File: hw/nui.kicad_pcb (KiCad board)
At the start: 2 copper layers, 50.8 x 71.1 mm, 24 parts, among them J1 D_PWR, J2 IR_RCV, J3 A_PWR, J4 Input, J5 Output, U1 Teensy-LC, U2 TC7660S, U3 PGA2311

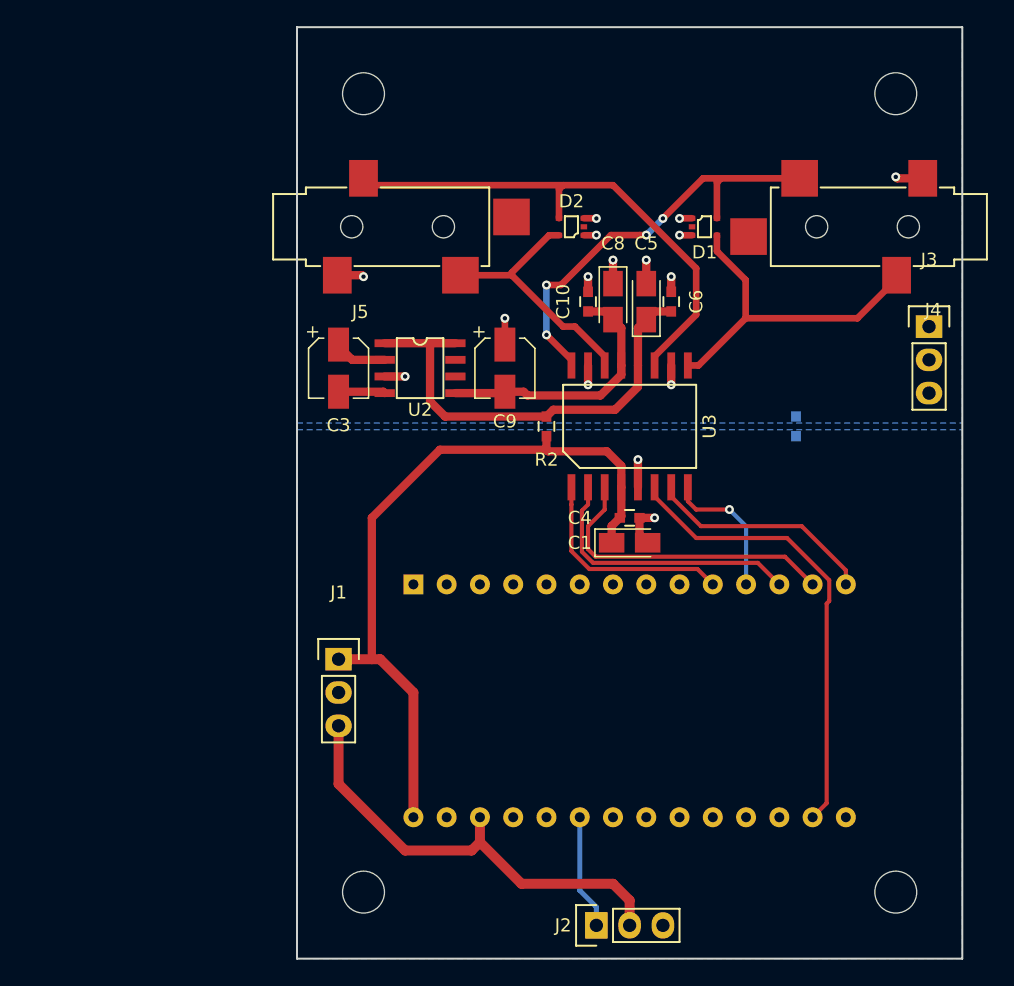
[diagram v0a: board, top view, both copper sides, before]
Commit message: Layout done for v0.0.1
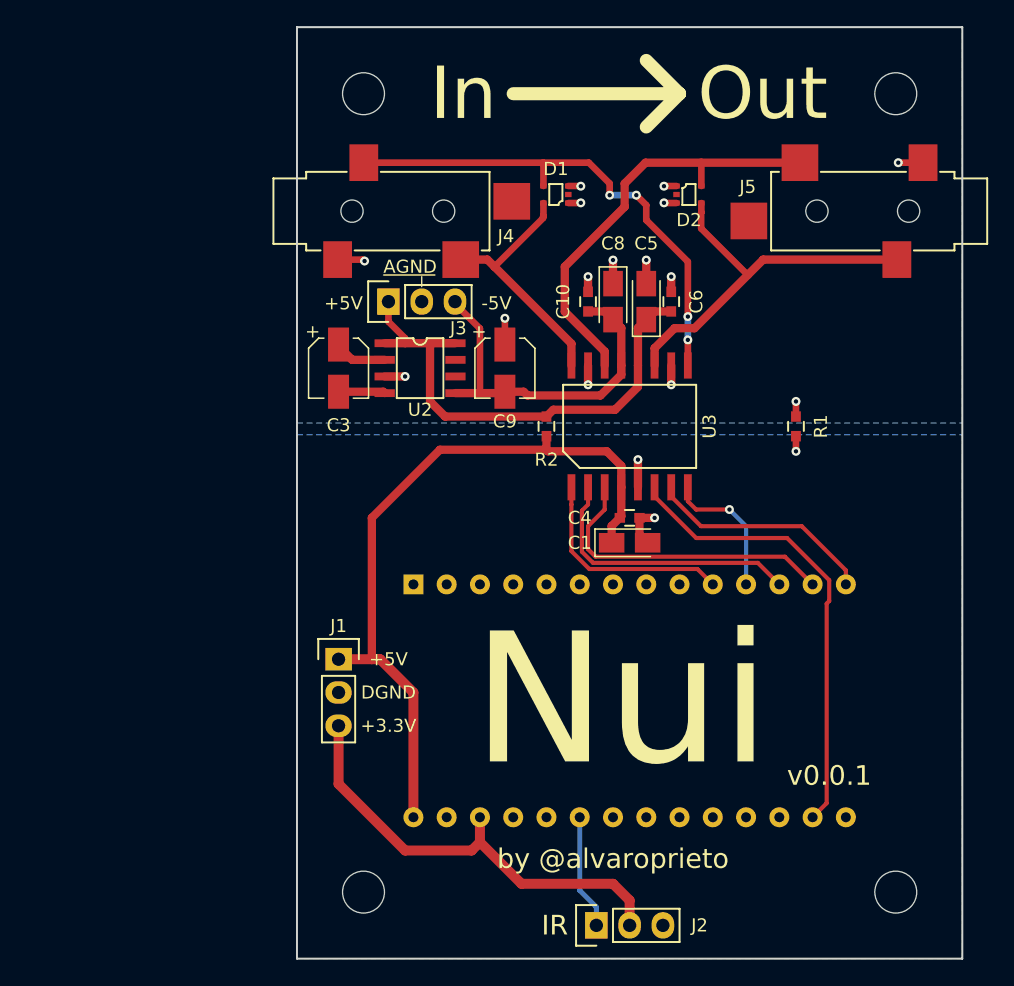
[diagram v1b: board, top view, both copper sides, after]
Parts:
- R1: moved to F.Cu
- moved J3 41.3 mm to (184.8, 76.8), turned to 90 degrees
- moved J5 35.5 mm to (221.0, 69.9), turned to 180 degrees
- moved J4 35.5 mm to (185.5, 69.9), turned to 0 degrees
- moved D1 11.6 mm to (197.6, 68.7), turned to 180 degrees
- moved D2 9.30 mm to (207.7, 68.7), turned to 0 degrees
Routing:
- net /VIN_L: track 32.8 -> 19.2 mm, vias 4 -> 0
- net /VOUT_L: track 19.3 -> 32.9 mm
- net /VIN_R: track 26.2 -> 38.8 mm, vias 0 -> 4
- net /VOUT_R: track 39.6 -> 29.6 mm
- net /VA_M: track 20.1 -> 27.9 mm
- net /VA_P: track 34.7 -> 38.4 mm
- net GNDD: track 5.43 -> 6.58 mm, vias 2 -> 3
- net GNDA: track 20.4 -> 21.4 mm, vias 14 -> 15
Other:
- board text added: "+3.3V"
- board text added: "+5V"
- board text added: "-5V"
- board text added: "AGND"
- board text added: "DGND"
- board text added: "IR"
- board text added: "In"
- board text added: "Nui"
- board text added: "Out"
- board text added: "by @alvaroprieto"
- board text added: "v0.0.1"

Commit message: Start updating pcb with new design
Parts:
- added C11: 2.2uF, Capacitors_SMD:C_0603, F.Cu at (186.2, 82.0)
- added C2: 4.7uF, Capacitors_SMD:C_0805, F.Cu at (194.6, 80.3)
- added C7: 2.2uF, Capacitors_SMD:C_0402_NoSilk, F.Cu at (183.9, 81.5)
- added R3: 10k, Resistors_SMD:R_0402_NoSilk, F.Cu at (180.9, 79.5)
- added R4: 1.74M, Resistors_SMD:R_0402_NoSilk, F.Cu at (183.4, 77.5)
- added R5: 549k, Resistors_SMD:R_0402_NoSilk, F.Cu at (183.4, 79.2)
- added R6: 511k, Resistors_SMD:R_0402_NoSilk, F.Cu at (181.9, 84.0)
- added R7: 1.58M, Resistors_SMD:R_0402_NoSilk, F.Cu at (181.9, 82.3)
- C3: value 10uF -> 1uF; footprint Capacitors_SMD:CP_Elec_4x5.3 -> Capacitors_SMD:C_1210
- C9: value 10uF -> 2.2uF; footprint Capacitors_SMD:CP_Elec_4x5.3 -> Capacitors_SMD:C_0603
- U2: value TC7660S -> LM27762; footprint alvarop:TC7660S-SOIC -> alvarop:LM27762
- moved J3 26.3 mm to (158.8, 73.2)
- moved C3 10.3 mm to (191.3, 81.3)
- moved C9 8.98 mm to (186.2, 77.0), turned to 180 degrees
- moved U2 2.62 mm to (186.2, 79.5)
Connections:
- C1 pad 1: /VD_P -> /EN+
- C4 pad 1: /VD_P -> /EN+
- C9 pad 1: GNDA -> /OUT+
- C9 pad 2: /VA_M -> GNDA
- J1 pad 1: /VD_P -> /EN+
- U1 pad 28: /VD_P -> /EN+
- U2 pad 1: /VA_P -> Net-(R3-Pad1)
- U2 pad 2: Net-(C3-Pad1) -> /FB+
- U2 pad 3: GNDA -> /EN+
- U2 pad 4: Net-(C3-Pad2) -> GNDA
- U2 pad 5: /VA_M -> Net-(C7-Pad1)
- U2 pad 6: Net-(U2-Pad6) -> /OUT-
- U2 pad 7: Net-(U2-Pad7) -> /FB-
- U2 pad 8: /VA_P -> /EN+
- U3 pad 4: /VD_P -> /EN+
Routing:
- net /VA_P: track 38.4 -> 15.5 mm
- net /VA_M: track 27.9 -> 8.87 mm
- net /VD_P: track 56.0 -> 37.8 mm
- net /EN+: track 0.00 -> 18.2 mm
- net Net-(C3-Pad1): track 4.13 -> 0.00 mm
- net Net-(C3-Pad2): track 3.69 -> 0.00 mm
- net GNDA: track 21.4 -> 17.9 mm, vias 15 -> 13

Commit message: Update Nui 1.0.0 to use nrf52810 and LM27762
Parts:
- added AE1: Antenna, alvarop:AMCA31-2R450G-S1F-T3, F.Cu at (202.7, 113.8)
- added C12: 0.1uF, Capacitors_SMD:C_0603, F.Cu at (208.0, 97.9)
- added C13: 0.1uF, Capacitors_SMD:C_0603, F.Cu at (199.4, 98.8)
- added C14: 4.7uF, Capacitors_SMD:C_0603, F.Cu at (208.0, 99.6)
- added C15: 1uF, Capacitors_SMD:C_0603, F.Cu at (208.0, 100.8)
- added C16: 0.1uF, Capacitors_SMD:C_0603, F.Cu at (208.0, 103.4)
- added C17: 12pf, Capacitors_SMD:C_0603, F.Cu at (208.0, 109.0)
- added C18: 100pf, Capacitors_SMD:C_0603, F.Cu at (205.0, 107.1)
- added C19: 12pf, Capacitors_SMD:C_0603, F.Cu at (208.0, 104.9)
- added C20: 1uF, Capacitors_SMD:C_0603, F.Cu at (187.1, 97.8)
- added C21: 1uF, Capacitors_SMD:C_0603, F.Cu at (192.5, 97.8)
- added C22: DNP, Capacitors_SMD:C_0402_NoSilk, F.Cu at (202.1, 108.0)
- added C23: DNP, Capacitors_SMD:C_0402_NoSilk, F.Cu at (202.1, 110.4)
- added D3: TVS, Diodes_SMD:D_0603, F.Cu at (184.4, 95.1)
- added F1: 2450FM07A0029T, alvarop:2450FM07A0029T, F.Cu at (202.7, 105.8)
- added J6: USB_OTG, alvarop:USB_MICRO_B, F.Cu at (181.9, 94.5)
- added J7: ARM-SWD, alvarop:ARM_SWD_SMD, B.Cu at (194.7, 104.5)
- added L1: Filter, Resistors_SMD:R_0603, F.Cu at (182.6, 100.6)
- added L2: Filter, Resistors_SMD:R_0603, F.Cu at (185.2, 92.8)
- added U4: MIC550X, alvarop:SOT-23(M5), F.Cu at (189.8, 97.9)
- added Y1: 32Mhz, Crystals:Crystal_SMD_2016-4pin_2.0x1.6mm, F.Cu at (208.0, 106.9)
- R2: footprint Capacitors_SMD:C_0603 -> Resistors_SMD:R_0402_NoSilk
- U1: value Teensy-LC -> NRF52810-QCAA; footprint alvarop:Teensy-LC -> alvarop:NRF52810_QCAA_QFN32; moved to F.Cu
- moved J3 37.5 mm to (195.6, 80.0), turned to 0 degrees
- moved J2 35.7 mm to (226.2, 99.4), turned to 180 degrees
- moved R2 23.6 mm to (202.7, 109.2)
- moved J1 16.4 mm to (186.9, 88.9), turned to 90 degrees
- moved C2 14.8 mm to (180.6, 85.0), turned to 180 degrees
- moved REF** 12.7 mm to (182.9, 109.2)
- moved REF** 12.7 mm to (223.5, 109.2)
- moved U1 5.72 mm to (203.5, 101.6)
- moved R6 4.70 mm to (186.6, 83.9), turned to 180 degrees
- moved R7 3.47 mm to (184.9, 83.9), turned to 180 degrees
- moved R4 2.95 mm to (186.3, 77.1), turned to 180 degrees
- moved R5 2.46 mm to (184.7, 77.1), turned to 180 degrees
- moved C3 2.05 mm to (189.4, 80.5)
- moved C9 1.42 mm to (185.5, 78.2)
- moved U2 1.20 mm to (185.5, 80.5)
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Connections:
- C11 pad 2: /OUT- -> /VA_M
- C9 pad 1: /OUT+ -> /VA_P
- R2 pad 1: /VA_P -> Net-(C22-Pad1)
- R2 pad 2: /VD_P -> Net-(AE1-Pad1)
- R4 pad 1: /OUT+ -> /VA_P
- R7 pad 2: /OUT- -> /VA_M
- U1 pad 1: GNDD -> Net-(C12-Pad1)
- U1 pad 10: /ZC_EN -> Net-(U1-Pad10)
- U1 pad 11: /MUTE_N -> Net-(U1-Pad11)
- U1 pad 12: /CS_N -> Net-(U1-Pad12)
- U1 pad 13: /MOSI -> Net-(U1-Pad13)
- U1 pad 14: /MISO -> Net-(U1-Pad14)
- U1 pad 16: /SCK -> /nRST
- U1 pad 17: Net-(U1-Pad17) -> /SWDCLK
- U1 pad 18: Net-(U1-Pad18) -> /SWDIO
- U1 pad 2: Net-(U1-Pad2) -> /MUTE_N
- U1 pad 20: Net-(U1-Pad20) -> GNDD
- U1 pad 23: /IR_IN -> Net-(C17-Pad1)
- U1 pad 25: Net-(U1-Pad25) -> +3V3
- U1 pad 26: +3V3 -> /IR_IN
- U1 pad 27: GNDD -> Net-(U1-Pad27)
- U1 pad 28: /EN+ -> Net-(U1-Pad28)
- U1 pad 3: Net-(U1-Pad3) -> /MISO
- U1 pad 4: Net-(U1-Pad4) -> /SCK
- U1 pad 6: Net-(U1-Pad6) -> /MOSI
- U1 pad 7: Net-(U1-Pad7) -> /CS_N
- U1 pad 8: Net-(U1-Pad8) -> /ZC_EN
- U1 pad 9: Net-(U1-Pad9) -> +3V3
- U2 pad 11: /OUT+ -> /VA_P
- U2 pad 6: /OUT- -> /VA_M
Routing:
- net /EN+: track 18.2 -> 65.8 mm, vias 0 -> 5
- net /VD_P: track 37.8 -> 0.00 mm
- net +3V3: track 34.7 -> 71.7 mm, vias 0 -> 6
- net GNDD: track 6.58 -> 36.1 mm, vias 3 -> 22
- net /SCK: track 35.3 -> 9.39 mm
- net /VA_M: track 8.87 -> 33.5 mm
- net /VA_P: track 15.5 -> 33.7 mm, vias 0 -> 2
- net Net-(J6-Pad6): track 0.00 -> 17.8 mm
- net /nRST: track 0.00 -> 14.3 mm, vias 0 -> 1
- net /MOSI: track 23.5 -> 9.73 mm
- net /IR_IN: track 8.78 -> 21.6 mm
- net /CS_N: track 21.2 -> 9.52 mm
- net GNDA: track 17.9 -> 27.6 mm, vias 13 -> 18
- net /MISO: track 17.4 -> 8.99 mm
- net /SWDIO: track 0.00 -> 8.22 mm, vias 0 -> 1
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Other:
- board size 50.8 x 71.1 mm -> 50.8 x 61 mm
- net class Default: via_dia 0.6858 -> 0.508; via_drill 0.3302 -> 0.254
- rule via_min_drill: 0.3302 -> 0.254
- rule via_min_size: 0.6858 -> 0.508
- board text added: "v1.0.0"
- board text removed: "v0.0.1"
